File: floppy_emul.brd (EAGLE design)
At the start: 79.7 x 35.5 mm, 30 parts, among them Q1 16MHz, U1 ATMEGA328P, U2 HEF4050B, U3 PCF8574T, U4 LM1117 3.3V

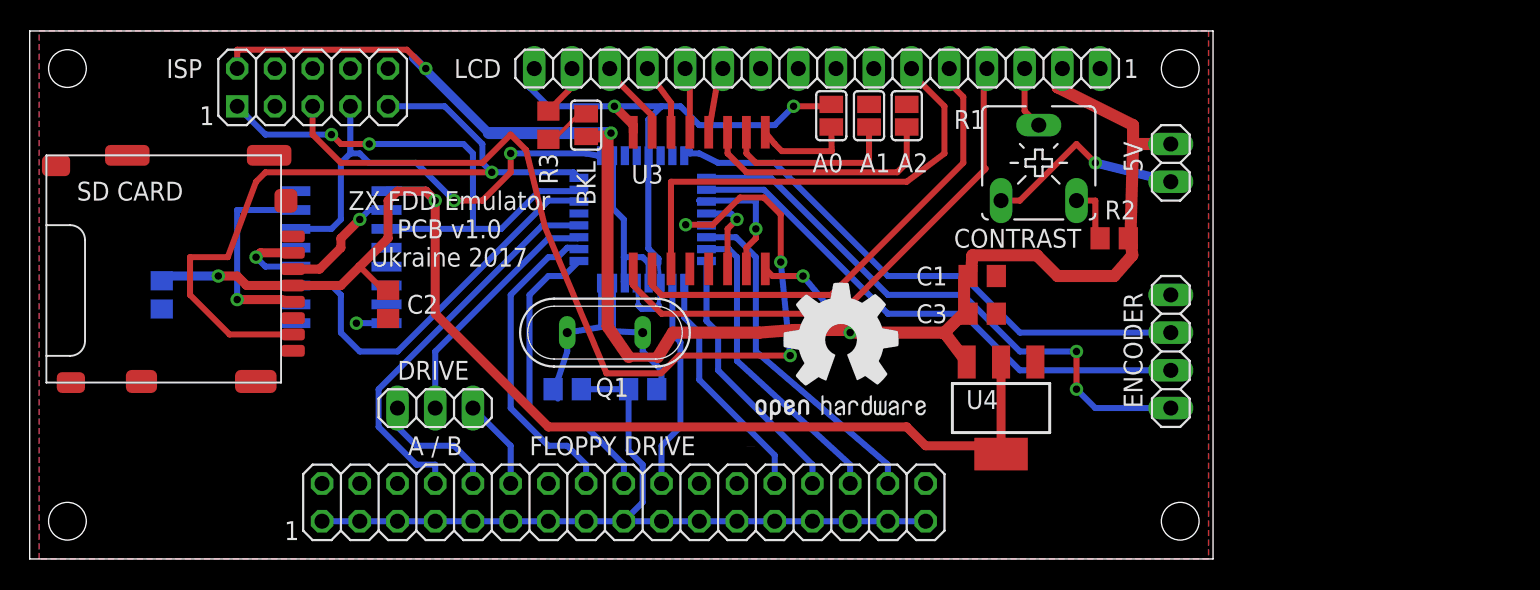
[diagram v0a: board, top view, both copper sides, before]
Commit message: Changed SD card connector, added SPI connector for external SD module
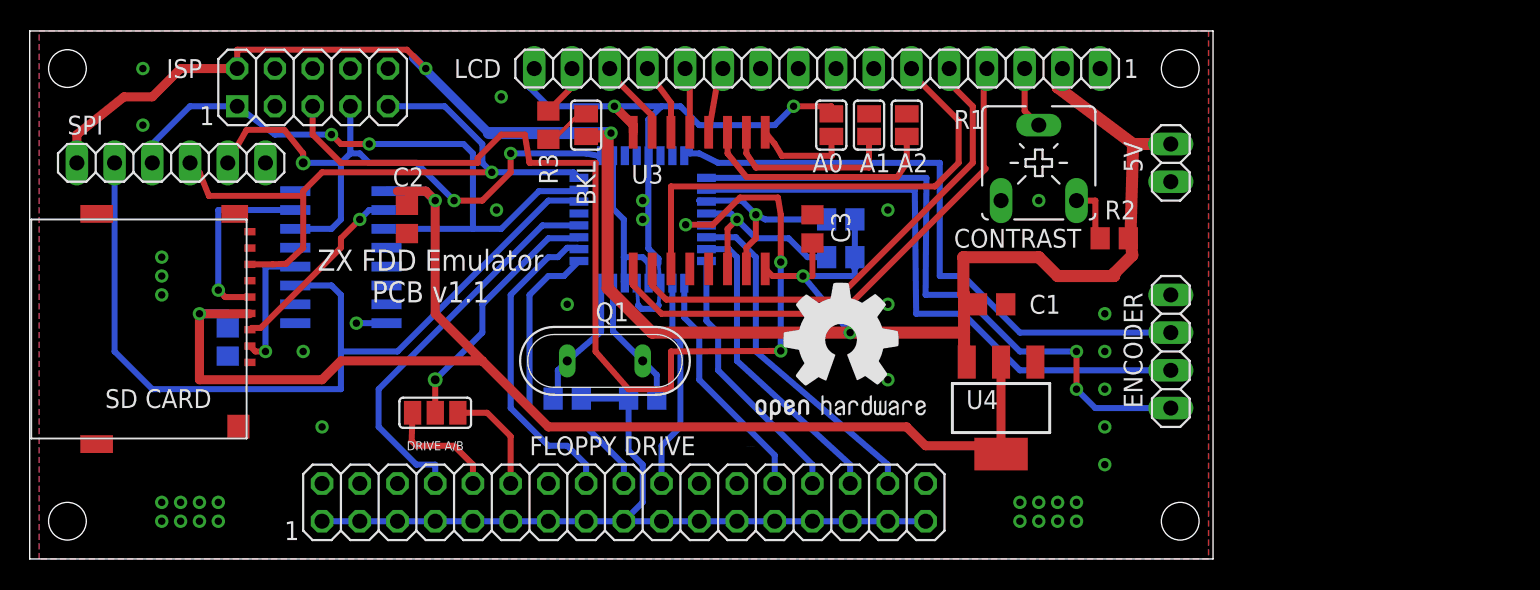
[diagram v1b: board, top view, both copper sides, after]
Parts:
- removed JP1: DRIVE SELECT, pinhead:1X03
- added CONN7: SPI, pinhead:1X06
- added R4, R5: 10k, rcl:R0805
- added SJ5: DRIVE SELECT, jumper:SJ_2
- CONN6: value MICRO SD -> MICROSD-PUSH-OUT; device con-molex-microsd:MICRO_SD_CONNECTOR -> microsd:MICROSD-PUSH-OUT
- moved C3 12.8 mm to (52.7, 22.2), turned to 90 degrees
- moved CONN6 5.99 mm to (14.6, 22.9)
- moved C2 5.85 mm to (25.4, 22.9)
- moved C4 5.46 mm to (13.3, 14.6)
- moved C1 2.01 mm to (64.8, 17.1)
- moved Q1 1.90 mm to (38.7, 13.3)
- moved C5 0.63 mm to (36.2, 10.8)
- moved C6 0.63 mm to (41.3, 10.8)
- moved SJ1 0.63 mm to (54.0, 29.2)
- moved SJ2 0.63 mm to (56.5, 29.2)
- moved SJ3 0.63 mm to (59.1, 29.2)
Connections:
- net CLK: now also CONN7.5
- net FDD_DRVSEL: now also SJ5.2; no longer JP1.2
- net FDD_DRVSEL0: now also SJ5.1; no longer JP1.1
- net FDD_DRVSEL1: now also SJ5.3; no longer JP1.3
- net GND: now also CONN6.G1, CONN6.G2, CONN6.G3, CONN6.G4, CONN7.6
- net MISO: now also CONN7.4
- net MOSI: now also CONN7.3
- net SCL: now also R4.1
- net SDA: now also R5.1
- net SDSEL: now also CONN7.2
- net VCC: now also CONN7.1, R4.2, R5.2
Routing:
- net SDSEL: track 26.7 -> 58.9 mm
- net VCC: track 130.8 -> 152.2 mm
- net GND: track 112.3 -> 98.4 mm, vias 4 -> 40
- net CLK: track 31.5 -> 41.8 mm, vias 2 -> 3
- net 3V3: track 84.9 -> 93.5 mm
- net MOSI: track 36.3 -> 44.2 mm
- net SCL: track 5.82 -> 12.9 mm
- net RESET: track 65.8 -> 71.9 mm
- net ENC_B: track 36.3 -> 41.1 mm
- net ENC_A: track 39.2 -> 43.8 mm
- net MISO: track 50.3 -> 45.6 mm
- net SD_MOSI: track 8.32 -> 12.9 mm
- net ENC_BTN: track 38.0 -> 42.5 mm
- net SDA: track 9.16 -> 13.4 mm
- net SD_SDSEL: track 5.51 -> 8.92 mm
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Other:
- board text added: "DRIVE A/B"
- board text added: "SPI"
- board text added: "ZX FDD Emulator PCB v1.1"
- board text removed: "A / B"
- board text removed: "DRIVE"
- board text removed: "ZX FDD Emulator PCB v1.0 Ukraine 2017"

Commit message: board v1.2
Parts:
- removed CONN6: MICROSD-PUSH-OUT, microsd:MICROSD-PUSH-OUT
- removed CONN7: SPI, pinhead:1X06
- removed SJ1: A0, jumper:SJ
- removed SJ2: A1, jumper:SJ
- removed SJ3: A2, jumper:SJ
- added J1: POWER_JACKPTH, SparkFun-Connectors:POWER_JACK_PTH
- added JP1: EXT SD CARD, pinhead:1X06
- added S1, S2, S3: (no value), switch-omron:B3F-10XX
- added SD1: ST-TF-003A, Seeed-Connector:MICRO-SD9+4P-SMD-16.1X14.5X1.85MM
- added SW1: ENCODER, piher:CI-11
- R1: device pot:CA6V -> pot:RJ9W
- moved U3 10.9 mm to (55.9, 25.4), turned to 90 degrees
- moved C3 6.54 mm to (55.9, 16.5), flipped to the bottom
- moved R2 4.49 mm to (72.4, 26.0)
- moved U4 4.49 mm to (69.8, 10.8)
- moved SJ4 3.86 mm to (36.8, 25.4), turned to 0 degrees
- moved R4 3.70 mm to (56.5, 23.5)
- moved R5 2.69 mm to (56.5, 21.0)
- moved SJ5 1.27 mm to (27.3, 11.1)
- moved R1 0.64 mm to (67.9, 26.0), turned to 270 degrees
- turned C1 to 90 degrees
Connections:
- removed net N$3: SJ1.2, U3.1
- removed net N$4: SJ2.2, U3.2
- removed net N$5: SJ3.2, U3.3
- new net LCD_LIGHT: U3.7
- net 3V3: now also JP1.3, SD1.4; no longer CONN6.4
- net CLK: no longer CONN7.5
- net ENC_A: now also S1.1, S1.2, SW1.A
- net ENC_B: now also S3.1, S3.2, SW1.B
- net ENC_BTN: now also S2.1, S2.2, SW1.D
- net GND: now also J1.GND, J1.GNDBREAK, JP1.5, S1.3, S1.4, S2.3, S2.4, S3.3, S3.4, SD1.6, SD1.G1, SD1.G2, SD1.G3, SD1.G4, SW1.C, SW1.E, U3.1, U3.2, U3.3; no longer CONN6.6, CONN6.G1, CONN6.G2, CONN6.G3, CONN6.G4, CONN7.6, SJ1.1, SJ2.1, SJ3.1
- net LCD_D4: now also U3.9; no longer U3.4
- net LCD_D5: now also U3.10; no longer U3.5
- net LCD_D6: now also U3.11; no longer U3.6
- net LCD_D7: now also U3.12; no longer U3.7
- net LCD_E: now also U3.6; no longer U3.11
- net LCD_RS: now also U3.4; no longer U3.9
- net LCD_RW: now also U3.5; no longer U3.10
- net MISO: now also JP1.6, SD1.7; no longer CONN6.7, CONN7.4
- net MOSI: no longer CONN7.3
- net SDSEL: no longer CONN7.2
- net SD_CLK: now also JP1.4, SD1.5; no longer CONN6.5
- net SD_MOSI: now also JP1.2, SD1.3; no longer CONN6.3
- net SD_SDSEL: now also JP1.1, SD1.2; no longer CONN6.2
- net VCC: now also J1.PWR; no longer CONN7.1
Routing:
- net ENC_B: track 41.1 -> 74.1 mm
- net SD_MOSI: track 12.9 -> 44.7 mm, vias 1 -> 3
- net SDSEL: track 58.9 -> 27.4 mm
- net ENC_A: track 43.8 -> 73.9 mm, vias 2 -> 1
- net GND: track 98.4 -> 68.7 mm, vias 40 -> 33
- net LCD_RS: track 36.7 -> 11.1 mm
- net LCD_E: track 33.4 -> 9.15 mm
- net LCD_RW: track 34.1 -> 10.4 mm
- net ENC_BTN: track 42.5 -> 64.6 mm
- net SD_SDSEL: track 8.92 -> 29.8 mm
- net N$5: track 16.5 -> 0.00 mm
- net 3V3: track 93.5 -> 107.2 mm
- net N$4: track 12.3 -> 0.00 mm
- net SD_CLK: track 12.9 -> 23.3 mm
- net CLK: track 41.8 -> 31.5 mm, vias 3 -> 2
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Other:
- board size 79.7 x 35.5 mm -> 99.4 x 35.5 mm
- board text added: "+"
- board text added: "-"
- board text added: "ZX FDD Emulator PCB v1.2"
- board text removed: "A0"
- board text removed: "A1"
- board text removed: "A2"
- board text removed: "SPI"
- board text removed: "ZX FDD Emulator PCB v1.1"
